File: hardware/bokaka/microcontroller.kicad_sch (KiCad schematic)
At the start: 12 parts, among them U2 STM32L053R8Tx

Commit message: Finalize design before pcb
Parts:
- removed R5: R, symbol Device:R
- C10, C11, C3, C4, C5, C6, C7, C8, C9: footprint (none) -> Capacitor_SMD:C_0402_1005Metric
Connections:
- net BUZZ_PWM: now also U2.22 (PA6); no longer U2.29 (PB10)
- net UART_RX: now also U2.43 (PA10); no longer U2.17 (PA3)
- net UART_TX: now also U2.42 (PA9); no longer U2.16 (PA2)
- net USR_BTN0: now also U2.34 (PB13); no longer U2.2 (PC13)
- net USR_BTN1: now also U2.35 (PB14); no longer U2.3 (PC14)
- net LED_USER: now reaches U2.21 (PA5)
- net LED_EN: now reaches U2.23 (PA7)
- net TAP_IO: now reaches U2.26 (PB0)
- net LED_DEBUG: now reaches U2.27 (PB1)
- net LED_STATUS renamed USB_DETECT
- net TAP_DATA: no longer names the net of U2.14 (PA0)
- net TAP_DETECT renamed TAP_WAKE
- no-connect marks 37 -> 34

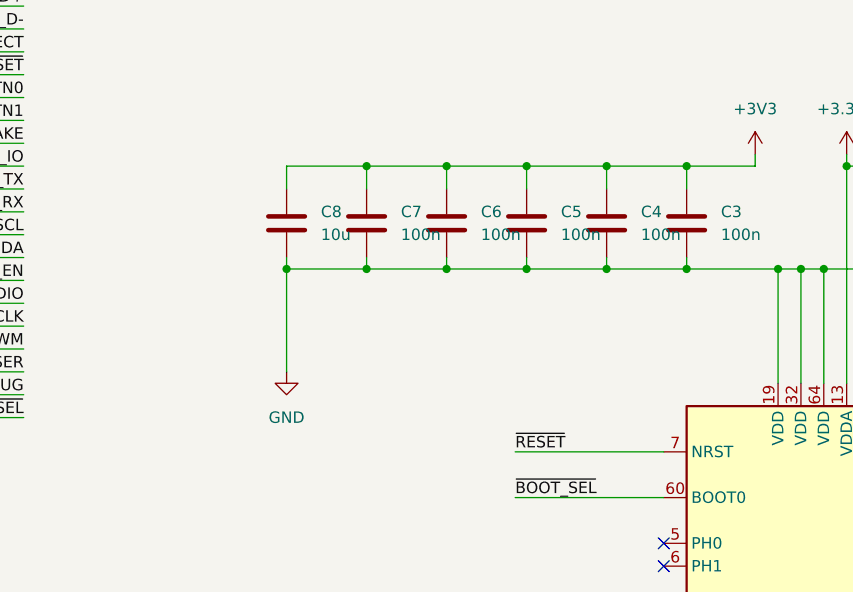
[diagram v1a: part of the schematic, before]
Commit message: footprint asignment
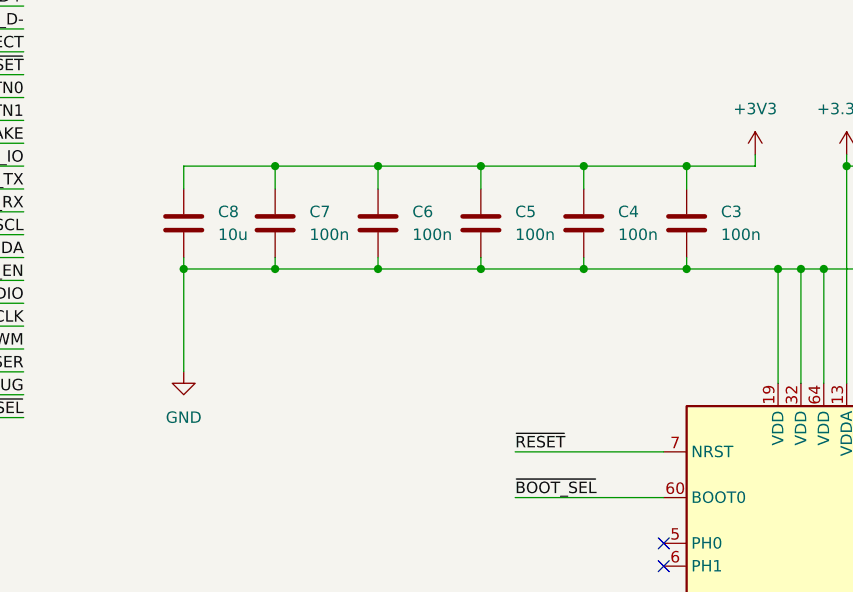
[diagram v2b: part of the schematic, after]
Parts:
- FB1: footprint (none) -> Inductor_SMD:L_0805_2012Metric
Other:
- moved on the sheet: C4, C5, C6, C7, C8

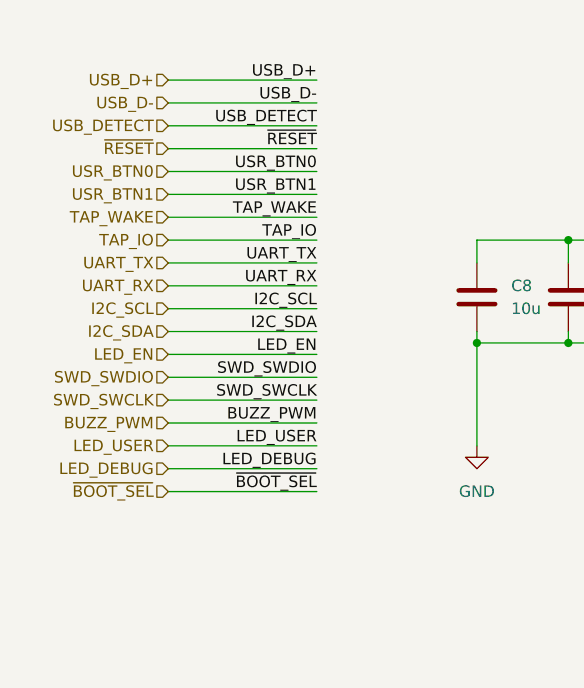
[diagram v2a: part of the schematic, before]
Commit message: schematic update
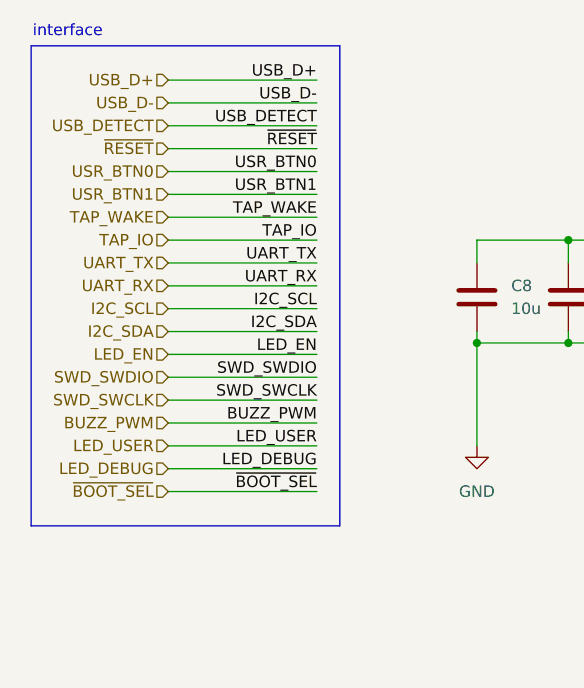
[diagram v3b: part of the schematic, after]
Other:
- note added: "interface"
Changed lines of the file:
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@@
 		(company "DIVA Engineering")
+	)
+	(rectangle
+		(start 16.51 25.4)
+		(end 50.8 78.74)
+		(stroke
+			(width 0)
+			(type default)
+		)
+		(fill
+			(type none)
+		)
+	)
+	(text "interface"
+		(exclude_from_sim no)
+		(at 20.574 23.876 0)
+		(effects
+			(font
+				(size 1.27 1.27)
+			)
+		)
 	)
 	(junction

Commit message: hardware update
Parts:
- added R14, R15: 1K8, Resistor_SMD:R_0402_1005Metric, symbol Device:R
- C10, C11: footprint Capacitor_SMD:C_0402_1005Metric -> Capacitor_SMD:C_0603_1608Metric
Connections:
- net +3V3: now also R14.1, R15.1
- net I2C_SCL: now also R15.2
- net I2C_SDA: now also R14.2

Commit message: Devkit Production Ready
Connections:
- net +3V3: now also U2.1 (VLCD), U2.19 (VDD), U2.32 (VDD), U2.48 (VDD_USB), U2.64 (VDD)
- net GND: no longer U2.1 (VLCD), U2.19 (VDD), U2.32 (VDD), U2.48 (VDD_USB), U2.64 (VDD)
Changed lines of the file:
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@@
+	)
+	(junction
+		(at 132.08 46.99)
+		(diameter 0)
+		(color 0 0 0 0)
 	)
 	(junction
@@
 		(color 0 0 0 0)
 	)
-	(junction
-		(at 121.92 58.42)
-		(diameter 0)
-		(color 0 0 0 0)
-	)
 	(no_connect
 		(at 154.94 88.9)
@@
 	(wire
 		(pts
+			(xy 132.08 46.99) (xy 132.08 58.42)
+		)
+		(stroke
+			(width 0)
+			(type default)
+		)
+	)
+	(wire
+		(pts
 			(xy 154.94 101.6) (xy 171.45 101.6)
 		)
@@
 	(wire
 		(pts
-			(xy 121.92 58.42) (xy 132.08 58.42)
-		)
-		(stroke
-			(width 0)
-			(type default)
-		)
-	)
-	(wire
-		(pts
 			(xy 76.2 57.15) (xy 76.2 58.42)
 		)
@@
 	(wire
 		(pts
-			(xy 121.92 46.99) (xy 129.54 46.99)
+			(xy 121.92 46.99) (xy 132.08 46.99)
 		)
 		(stroke
@@
 	(wire
 		(pts
-			(xy 129.54 45.72) (xy 129.54 46.99)
+			(xy 132.08 45.72) (xy 132.08 46.99)
 		)
 		(stroke
@@
 	(symbol
 		(lib_id "power:+3V3")
-		(at 129.54 45.72 0)
+		(at 132.08 45.72 0)
 		(unit 1)
 		(exclude_from_sim no)
@@
 		(fields_autoplaced yes)
 		(property "Reference" "#PWR03"
-			(at 129.54 49.53 0)
+			(at 132.08 49.53 0)
 			(effects
 				(font
@@
 		)
 		(property "Value" "+3V3"
-			(at 129.54 40.64 0)
+			(at 132.08 40.64 0)
 			(effects
 				(font
@@
 		)
 		(property "Footprint" ""
-			(at 129.54 45.72 0)
+			(at 132.08 45.72 0)
 			(effects
 				(font
@@
 		)
 		(property "Datasheet" ""
-			(at 129.54 45.72 0)
+			(at 132.08 45.72 0)
 			(effects
 				(font
@@
 		)
 		(property "Description" "Power symbol creates a global label with name \"+3V3\""
-			(at 129.54 45.72 0)
-			(effects
-				(font
+			(at 132.08 45.72 0)
+			(effects
+				(font
